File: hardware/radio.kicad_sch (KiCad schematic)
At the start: 3 parts, among them U2 Ai-Thinker-Ra-02

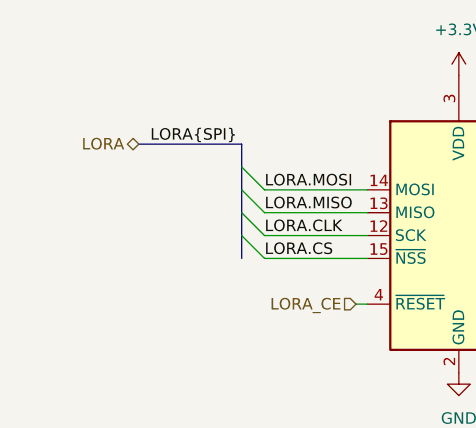
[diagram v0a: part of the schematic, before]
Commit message: Route all board
Fix CS missing for SD card
Add IMU symbol and footprint to the project lib
Finish esp32 pinswaps
Move non critical signals to the keyboard IO expander
Add power flag symbols
Fix Dpad pin type
Fix IMU pin type
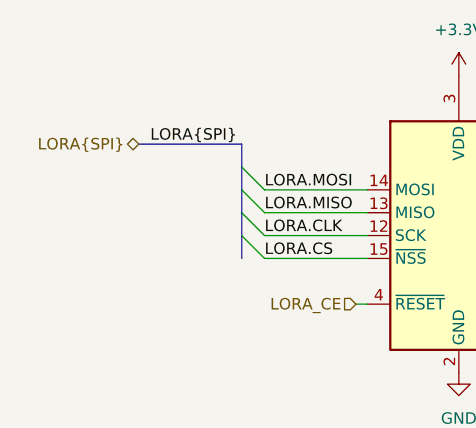
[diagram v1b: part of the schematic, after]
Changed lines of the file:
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@@
 		)
 	)
-	(hierarchical_label "LORA"
+	(hierarchical_label "LORA{SPI}"
 		(shape bidirectional)
 		(at 105.41 83.82 180)

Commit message: Associate all LCSC component
Change sdcard pullup resistor to 47K
Center main schematic
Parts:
- C11: LCSC (none) -> C1691
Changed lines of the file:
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@@
+			)
+		)
+		(property "LCSC" "C1691"
+			(at 160.02 127 0)
+			(effects
+				(font
+					(size 1.27 1.27)
+				)
+				(hide yes)
 			)
 		)

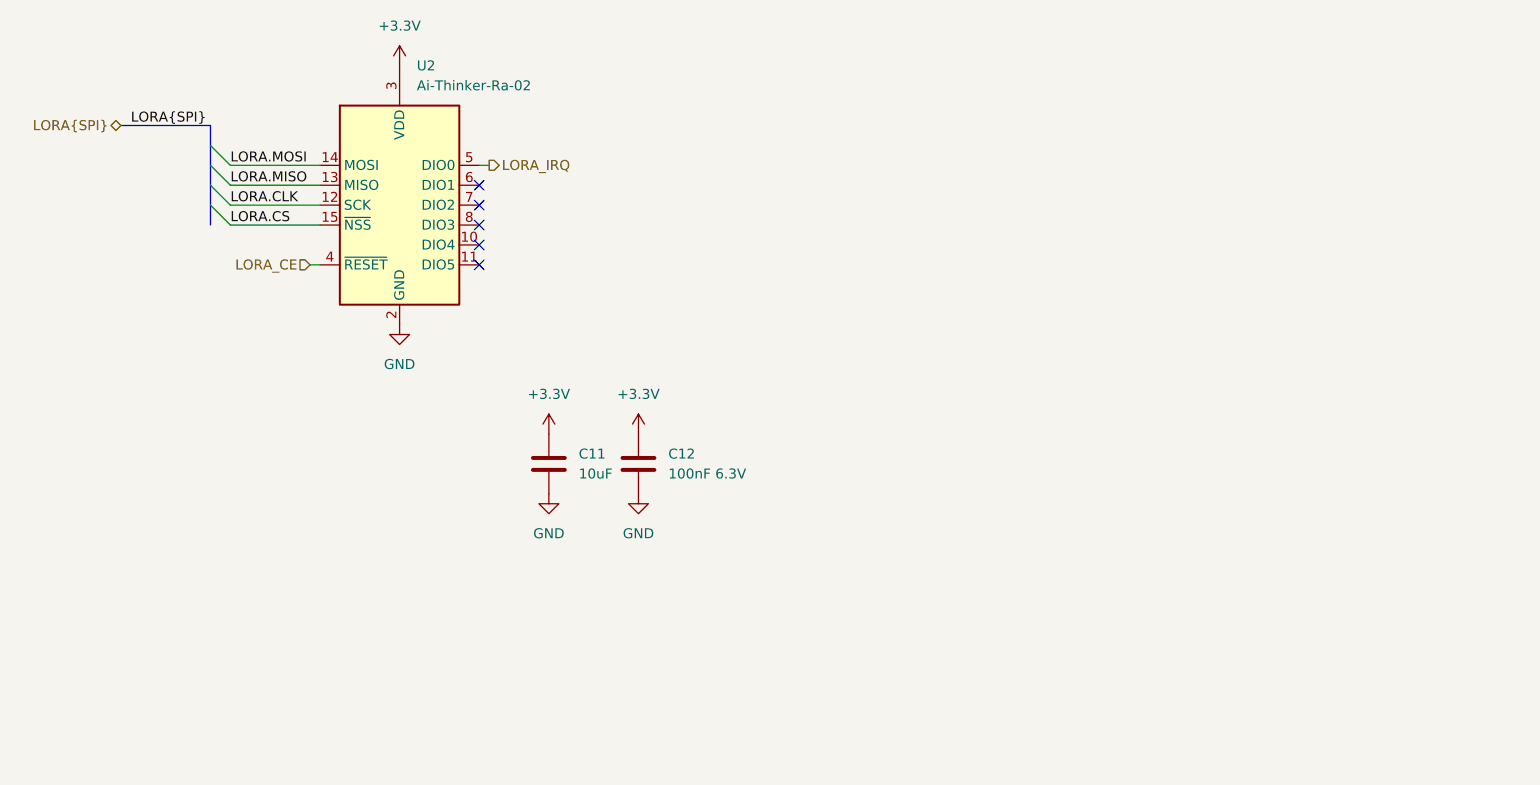
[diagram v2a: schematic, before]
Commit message: Beautified schematic, added I2C addresses
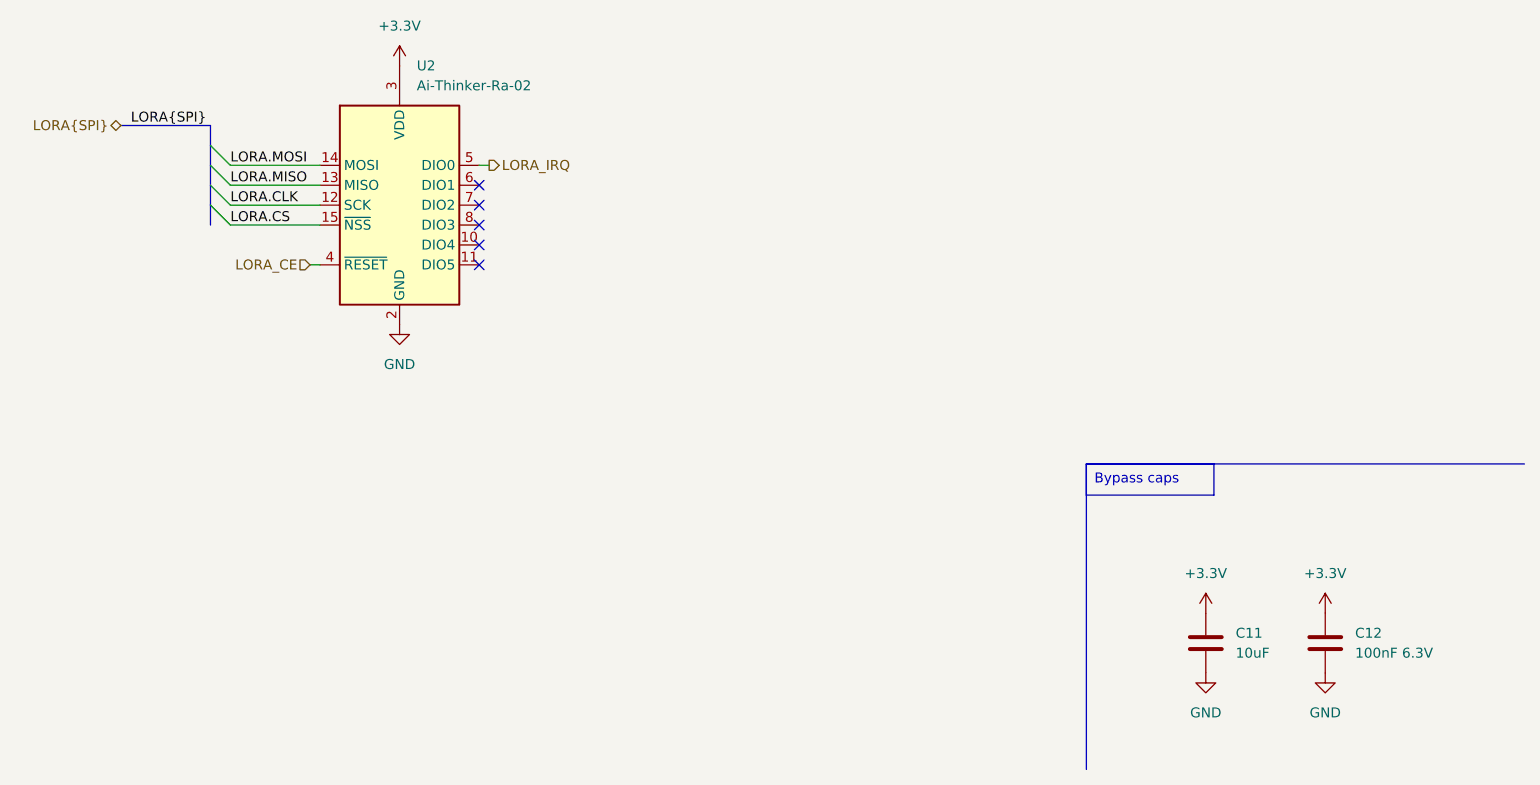
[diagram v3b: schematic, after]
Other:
- moved on the sheet: C11, C12
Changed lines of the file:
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@@
+		)
+	)
+	(polyline
+		(pts
+			(xy 228.6 165.9789) (xy 228.6 127)
+		)
+		(stroke
+			(width 0)
+			(type default)
 		)
 	)
@@
 		)
 	)
+	(polyline
+		(pts
+			(xy 228.6 127) (xy 284.48 127)
+		)
+		(stroke
+			(width 0)
+			(type default)
+		)
+	)
 	(bus
 		(pts
@@
 		)
 	)
-	(label "LORA{SPI}"
-		(at 106.68 83.82 0)
-		(fields_autoplaced yes)
+	(text_box "Bypass caps"
+		(exclude_from_sim no)
+		(at 228.6 127 0)
+		(size 16.2714 3.98)
+		(stroke
+			(width 0)
+			(type default)
+		)
+		(fill
+			(type none)
+		)
 		(effects
 			(font
 				(size 1.27 1.27)
 			)
-			(justify left bottom)
-		)
-	)
-	(label "LORA.MOSI"
-		(at 119.38 88.9 0)
+			(justify left top)
+		)
+	)
+	(label "LORA{SPI}"
+		(at 106.68 83.82 0)
 		(fields_autoplaced yes)
 		(effects
@@
 		)
 	)
-	(label "LORA.CS"
-		(at 119.38 96.52 0)
+	(label "LORA.MOSI"
+		(at 119.38 88.9 0)
 		(fields_autoplaced yes)
 		(effects
@@
 		)
 	)
-	(label "LORA.CLK"
-		(at 119.38 93.98 0)
+	(label "LORA.CS"
+		(at 119.38 96.52 0)
 		(fields_autoplaced yes)
 		(effects
@@
 		)
 	)
-	(label "LORA.MISO"
-		(at 119.38 91.44 0)
+	(label "LORA.CLK"
+		(at 119.38 93.98 0)
 		(fields_autoplaced yes)
 		(effects
@@
 		)
 	)
+	(label "LORA.MISO"
+		(at 119.38 91.44 0)
+		(fields_autoplaced yes)
+		(effects
+			(font
+				(size 1.27 1.27)
+			)
+			(justify left bottom)
+		)
+	)
 	(hierarchical_label "LORA_IRQ"
 		(shape output)
@@
 	(symbol
 		(lib_id "power:GND")
-		(at 160.02 130.81 0)
+		(at 243.84 153.67 0)
 		(unit 1)
 		(exclude_from_sim no)
@@
 		(fields_autoplaced yes)
 		(property "Reference" "#PWR082"
-			(at 160.02 137.16 0)
+			(at 243.84 160.02 0)
 			(effects
 				(font
@@
 		)
 		(property "Value" "GND"
-			(at 160.02 135.89 0)
+			(at 243.84 158.75 0)
 			(effects
 				(font
@@
 		)
 		(property "Footprint" ""
-			(at 160.02 130.81 0)
+			(at 243.84 153.67 0)
 			(effects
 				(font
@@
 		)
 		(property "Datasheet" ""
-			(at 160.02 130.81 0)
+			(at 243.84 153.67 0)
 			(effects
 				(font
@@
 		)
 		(property "Description" "Power symbol creates a global label with name \"GND\" , ground"
-			(at 160.02 130.81 0)
+			(at 243.84 153.67 0)
 			(effects
 				(font
@@
 	(symbol
 		(lib_id "power:GND")
-		(at 171.45 130.81 0)
+		(at 259.08 153.67 0)
 		(unit 1)
 		(exclude_from_sim no)
@@
 		(fields_autoplaced yes)
 		(property "Reference" "#PWR084"
-			(at 171.45 137.16 0)
+			(at 259.08 160.02 0)
 			(effects
 				(font
@@
 		)
 		(property "Value" "GND"
-			(at 171.45 135.89 0)
+			(at 259.08 158.75 0)
 			(effects
 				(font
@@
 		)
 		(property "Footprint" ""
-			(at 171.45 130.81 0)
+			(at 259.08 153.67 0)
 			(effects
 				(font
@@
 		)
 		(property "Datasheet" ""
-			(at 171.45 130.81 0)
+			(at 259.08 153.67 0)
 			(effects
 				(font
@@
 		)
 		(property "Description" "Power symbol creates a global label with name \"GND\" , ground"
-			(at 171.45 130.81 0)
+			(at 259.08 153.67 0)
 			(effects
 				(font
@@
 	(symbol
 		(lib_id "Device:C")
-		(at 160.02 127 0)
+		(at 243.84 149.86 0)
 		(unit 1)
 		(exclude_from_sim no)
@@
 		(fields_autoplaced yes)
 		(property "Reference" "C11"
-			(at 163.83 125.7299 0)
+			(at 247.65 148.5899 0)
 			(effects
 				(font
@@
 		)
 		(property "Value" "10uF"
-			(at 163.83 128.2699 0)
+			(at 247.65 151.1299 0)
 			(effects
 				(font
@@
 		)
 		(property "Footprint" "Capacitor_SMD:C_0603_1608Metric"
-			(at 160.9852 130.81 0)
+			(at 244.8052 153.67 0)
 			(effects
 				(font
@@
 		)
 		(property "Datasheet" "~"
-			(at 160.02 127 0)
+			(at 243.84 149.86 0)
 			(effects
 				(font
@@
 		)
 		(property "Description" "Unpolarized capacitor"
-			(at 160.02 127 0)
+			(at 243.84 149.86 0)
 			(effects
 				(font
@@
 		)
 		(property "LCSC" "C1691"
-			(at 160.02 127 0)
+			(at 243.84 149.86 0)
 			(effects
 				(font
@@
 	(symbol
 		(lib_id "Device:C")
-		(at 171.45 127 0)
+		(at 259.08 149.86 0)
 		(unit 1)
 		(exclude_from_sim no)
@@
 		(fields_autoplaced yes)
 		(property "Reference" "C12"
-			(at 175.26 125.7299 0)
+			(at 262.89 148.5899 0)
 			(effects
 				(font
@@
 		)
 		(property "Value" "100nF 6.3V"
-			(at 175.26 128.2699 0)
+			(at 262.89 151.1299 0)
 			(effects
 				(font
@@
 		)
 		(property "Footprint" "Capacitor_SMD:C_0402_1005Metric"
-			(at 172.4152 130.81 0)
+			(at 260.0452 153.67 0)
 			(effects
 				(font
@@
 		)
 		(property "Datasheet" "~"
-			(at 171.45 127 0)
+			(at 259.08 149.86 0)
 			(effects
 				(font
@@
 		)
 		(property "Description" "Unpolarized capacitor"
-			(at 171.45 127 0)
+			(at 259.08 149.86 0)
 			(effects
 				(font
@@
 		)
 		(property "LCSC" "C1525"
-			(at 171.45 127 0)
+			(at 259.08 149.86 0)
 			(effects
 				(font
@@
 	(symbol
 		(lib_id "power:+3.3V")
-		(at 171.45 123.19 0)
+		(at 259.08 146.05 0)
 		(unit 1)
 		(exclude_from_sim no)
@@
 		(fields_autoplaced yes)
 		(property "Reference" "#PWR083"
-			(at 171.45 127 0)
+			(at 259.08 149.86 0)
 			(effects
 				(font
@@
 		)
 		(property "Value" "+3.3V"
-			(at 171.45 118.11 0)
+			(at 259.08 140.97 0)
 			(effects
 				(font
@@
 		)
 		(property "Footprint" ""
-			(at 171.45 123.19 0)
+			(at 259.08 146.05 0)
 			(effects
 				(font
@@
 		)
 		(property "Datasheet" ""
-			(at 171.45 123.19 0)
+			(at 259.08 146.05 0)
 			(effects
 				(font
@@
 		)
 		(property "Description" "Power symbol creates a global label with name \"+3.3V\""
-			(at 171.45 123.19 0)
+			(at 259.08 146.05 0)
 			(effects
 				(font
@@
 	(symbol
 		(lib_id "power:+3.3V")
-		(at 160.02 123.19 0)
+		(at 243.84 146.05 0)
 		(unit 1)
 		(exclude_from_sim no)
@@
 		(fields_autoplaced yes)
 		(property "Reference" "#PWR081"
-			(at 160.02 127 0)
+			(at 243.84 149.86 0)
 			(effects
 				(font
@@
 		)
 		(property "Value" "+3.3V"
-			(at 160.02 118.11 0)
+			(at 243.84 140.97 0)
 			(effects
 				(font
@@
 		)
 		(property "Footprint" ""
-			(at 160.02 123.19 0)
+			(at 243.84 146.05 0)
 			(effects
 				(font
@@
 		)
 		(property "Datasheet" ""
-			(at 160.02 123.19 0)
+			(at 243.84 146.05 0)
 			(effects
 				(font
@@
 		)
 		(property "Description" "Power symbol creates a global label with name \"+3.3V\""
-			(at 160.02 123.19 0)
-			(effects
-				(font
+			(at 243.84 146.05 0)
+			(effects
+				(font

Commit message: update bom, correct jlcpcb rotation
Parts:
- U2: JLCPCB Rotation Offset (none) -> 90
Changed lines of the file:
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@@
+			)
+		)
+		(property "JLCPCB Rotation Offset" "90"
+			(at 140.97 93.98 0)
+			(effects
+				(font
+					(size 1.27 1.27)
+				)
+				(hide yes)
 			)
 		)

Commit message: Fix rotation and position offset of components
Fix lora module rotation
Fix esp32 module position offset
Fix sd card position offset
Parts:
- U2: JLCPCB Rotation Offset 90 -> 270
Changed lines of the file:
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@@
+			)
+		)
+		(property "JLCPCB Position Offset" ""
+			(at 243.84 149.86 0)
+			(effects
+				(font
+					(size 1.27 1.27)
+				)
+				(hide yes)
 			)
 		)
@@
 			)
 		)
-		(property "JLCPCB Rotation Offset" "90"
+		(property "JLCPCB Rotation Offset" "270"
+			(at 140.97 93.98 0)
+			(effects
+				(font
+					(size 1.27 1.27)
+				)
+				(hide yes)
+			)
+		)
+		(property "JLCPCB Position Offset" ""
 			(at 140.97 93.98 0)
 			(effects
@@
 			(at 259.08 149.86 0)
 			(effects
+				(font
+					(size 1.27 1.27)
+				)
+				(hide yes)
+			)
+		)
+		(property "JLCPCB Position Offset" ""
+			(at 259.08 149.86 0)
+			(effects

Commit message: update lcsc codes to use (new?) basic components
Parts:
- C11: LCSC C1691 -> C19702
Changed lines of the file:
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@@
 			)
 		)
-		(property "LCSC" "C1691"
+		(property "LCSC" "C19702"
 			(at 243.84 149.86 0)
 			(effects
